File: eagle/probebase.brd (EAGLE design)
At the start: 20 x 20 mm, 11 parts, among them M1 TPTP14R, M2 TPTP14R, M3 TPTP14R, P1- TPTP14R, P2- TPTP14R, P3- TPTP14R, P4- TPTP14R

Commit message: full probe demo except for lights and antenna
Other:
- outline, holes or cut-outs redrawn
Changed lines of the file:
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@@
 <plain>
 <circle x="10" y="10" radius="10" width="0.1524" layer="20"/>
-<wire x1="3" y1="9" x2="3" y2="12" width="0.1524" layer="20"/>
-<wire x1="3" y1="12" x2="17" y2="12" width="0.1524" layer="20"/>
-<wire x1="17" y1="12" x2="17" y2="9" width="0.1524" layer="20"/>
-<wire x1="17" y1="9" x2="3" y2="9" width="0.1524" layer="20"/>
 </plain>
 <attributes>

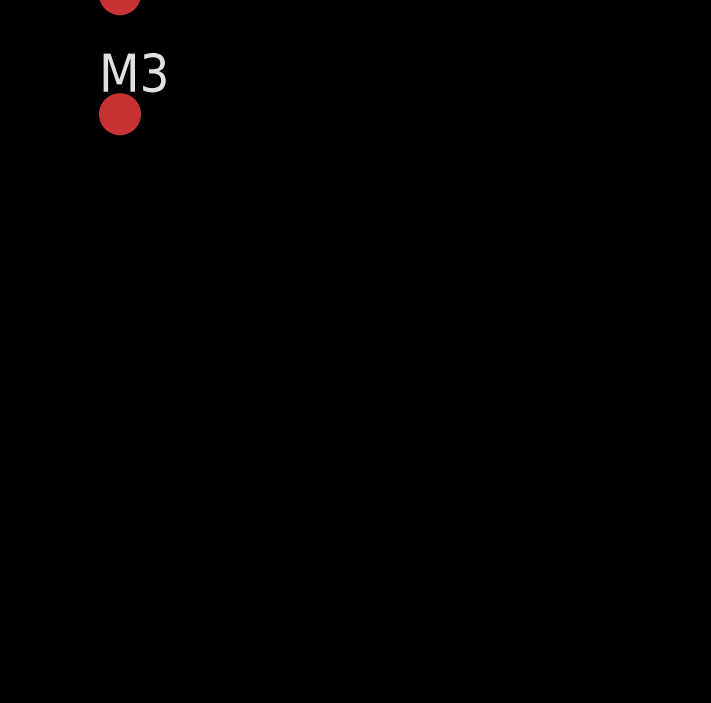
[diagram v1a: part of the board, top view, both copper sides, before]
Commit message: decided on ffc wire layout.
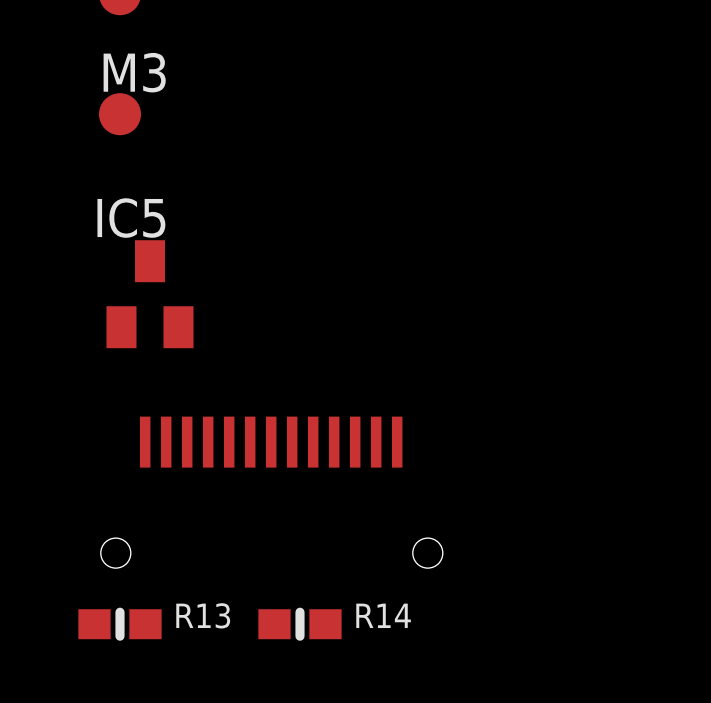
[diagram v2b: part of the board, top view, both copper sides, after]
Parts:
- added IC5: APX803, adafruit:SOT23
- added R13: 10K, microbuilder:0603-NO
- added R14: 22, microbuilder:0603-NO
- added U$4: TFT, general:MICROBUILDER_TFT_1.14IN_240X135_WRAPUNDER
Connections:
- new net !TFTRST: IC5.2, R13.1
- new net DC: U$4.5
- new net MOSI: U$4.3
- new net N$1: R14.2, U$4.11
- new net SCK: U$4.4
- new net TFTCS: U$4.7
- new net TFTRST: U$4.6
- net 3V: now also IC5.3, R13.2, U$4.10, U$4.12
- net GND: now also IC5.1, R14.1, U$4.13, U$4.8
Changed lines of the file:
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@@
 </variantdefs>
 <classes>
-<class number="0" name="default" width="0" drill="0">
+<class number="0" name="default" width="0.1524" drill="0">
+<clearance class="0" value="0.1524"/>
+</class>
+<class number="1" name="battery" width="0.3048" drill="0">
+<clearance class="1" value="0.1524"/>
 </class>
 </classes>
@@
 <attribute name="VALUE" x="0.492" y="-36.762" size="0.0254" layer="27"/>
 </element>
+<element name="IC5" library="adafruit" package="SOT23" value="APX803" x="2" y="-42" smashed="yes">
+<attribute name="NAME" x="0.095" y="-40.095" size="1.27" layer="25"/>
+<attribute name="VALUE" x="0.095" y="-45.175" size="1.27" layer="27"/>
+</element>
+<element name="R13" library="microbuilder" package="0603-NO" value="10K" x="1" y="-53" smashed="yes">
+<attribute name="NAME" x="2.778" y="-53.127" size="0.8128" layer="25" font="vector" ratio="18"/>
+<attribute name="VALUE" x="2.778" y="-53.762" size="0.4064" layer="27" font="vector" ratio="10"/>
+</element>
+<element name="R14" library="microbuilder" package="0603-NO" value="22" x="7" y="-53" smashed="yes">
+<attribute name="NAME" x="8.778" y="-53.127" size="0.8128" layer="25" font="vector" ratio="18"/>
+<attribute name="VALUE" x="8.778" y="-53.762" size="0.4064" layer="27" font="vector" ratio="10"/>
+</element>
+<element name="U$4" library="general" package="MICROBUILDER_TFT_1.14IN_240X135_WRAPUNDER" value="TFT" x="6" y="-49" smashed="yes"/>
 </elements>
 <signals>
@@
 <wire x1="15" y1="6.25" x2="15" y2="7" width="0.1524" layer="16"/>
 <via x="15" y="7" extent="1-16" drill="0.35"/>
+<contactref element="IC5" pad="1"/>
+<contactref element="U$4" pad="8"/>
+<contactref element="U$4" pad="13"/>
+<contactref element="R14" pad="1"/>
+<wire x1="5.34" y1="-46.93" x2="1.84" y2="-46.93" width="0" layer="19" extent="1-1"/>
+<wire x1="1.05" y1="-43.1" x2="1.84" y2="-46.93" width="0" layer="19" extent="1-1"/>
+<wire x1="6.15" y1="-53" x2="5.34" y2="-46.93" width="0" layer="19" extent="1-1"/>
+<wire x1="4.5" y1="5.75" x2="1.05" y2="-43.1" width="0" layer="19" extent="1-16"/>
+<wire x1="15" y1="7" x2="4.5" y2="5.75" width="0" layer="19" extent="16-16"/>
 </signal>
 <signal name="3V">
 <contactref element="LED1" pad="A"/>
 <contactref element="3V" pad="TP"/>
-<wire x1="1" y1="-4" x2="11.27" y2="16" width="0" layer="19" extent="1-1"/>
+<contactref element="R13" pad="2"/>
+<contactref element="IC5" pad="3"/>
+<contactref element="U$4" pad="12"/>
+<contactref element="U$4" pad="10"/>
+<wire x1="2.54" y1="-46.93" x2="1.85" y2="-53" width="0" layer="19" extent="1-1"/>
+<wire x1="3.94" y1="-46.93" x2="2.54" y2="-46.93" width="0" layer="19" extent="1-1"/>
+<wire x1="2" y1="-40.9" x2="2.54" y2="-46.93" width="0" layer="19" extent="1-1"/>
+<wire x1="1" y1="-4" x2="2" y2="-40.9" width="0" layer="19" extent="1-1"/>
+<wire x1="11.27" y1="16" x2="1" y2="-4" width="0" layer="19" extent="1-1"/>
 </signal>
 <signal name="P4-">
@@
 <contactref element="M3" pad="TP"/>
 </signal>
+<signal name="TFTCS">
+<contactref element="U$4" pad="7"/>
+</signal>
+<signal name="TFTRST">
+<contactref element="U$4" pad="6"/>
+</signal>
+<signal name="DC">
+<contactref element="U$4" pad="5"/>
+</signal>
+<signal name="SCK">
+<contactref element="U$4" pad="4"/>
+</signal>
+<signal name="MOSI">
+<contactref element="U$4" pad="3"/>
+</signal>
+<signal name="!TFTRST">
+<contactref element="IC5" pad="2"/>
+<contactref element="R13" pad="1"/>
+<wire x1="2.95" y1="-43.1" x2="0.15" y2="-53" width="0" layer="19" extent="1-1"/>
+</signal>
+<signal name="N$1">
+<contactref element="R14" pad="2"/>
+<contactref element="U$4" pad="11"/>
+<wire x1="3.24" y1="-46.93" x2="7.85" y2="-53" width="0" layer="19" extent="1-1"/>
+</signal>
 </signals>

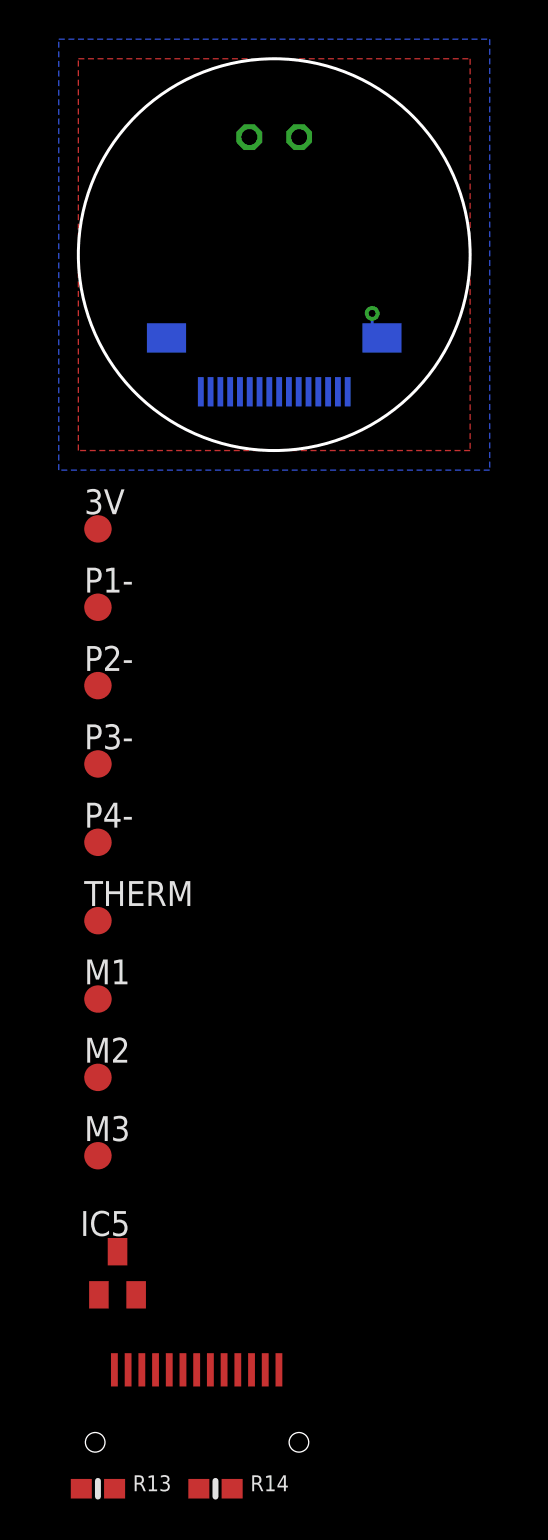
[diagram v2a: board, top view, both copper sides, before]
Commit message: First order of probe, probebase and FFC breakout PCBs for 22mm enclosure
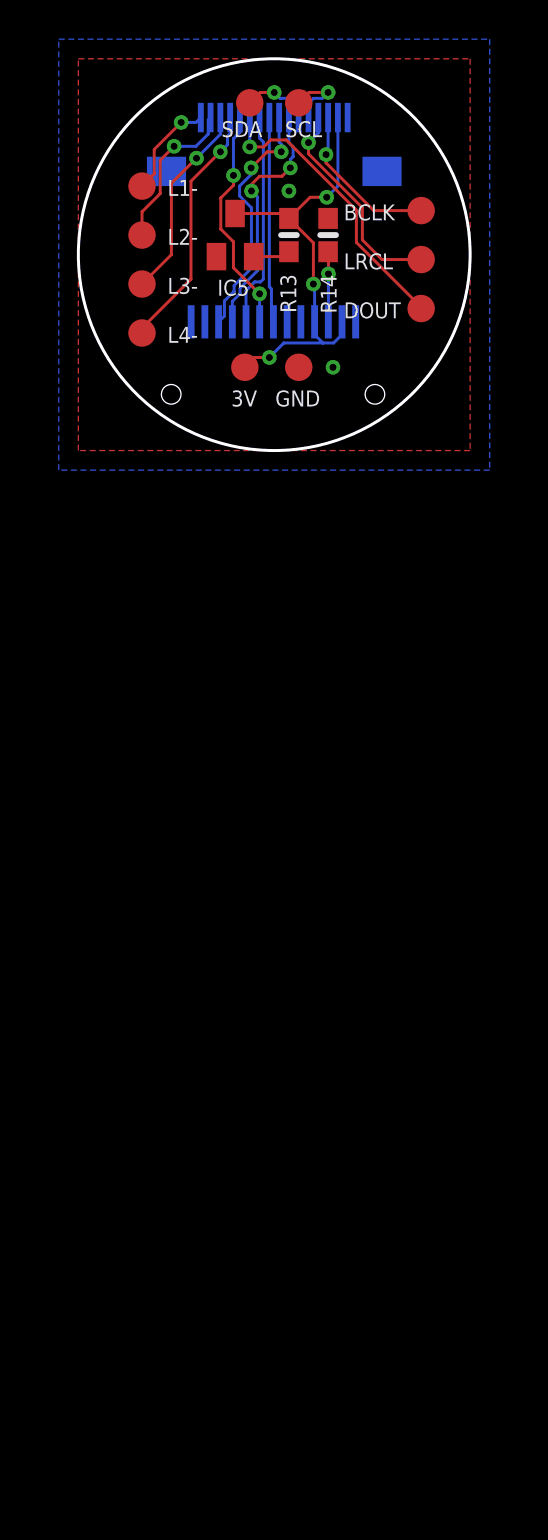
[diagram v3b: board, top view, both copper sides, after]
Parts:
- removed LED1: (no value), led:LED3MM
- removed M1, M2, M3, P1-, P2-, P3-, P4-, THERM: TPTP14R, testpad:TP14R
- removed U$1: 16PINFFC, general:16PINFFC
- added BCLK, DOUT, GND, L1-, L2-, L3-, L4-, LRCL, SCL, SDA: TPTP14R, testpad:TP14R
- added U$3: 16PINFFC, general:16PINFFC
- moved R13 64.7 mm to (10.8, 11.0), turned to 90 degrees
- moved R14 64.3 mm to (12.8, 11.0), turned to 270 degrees
- moved U$4 53.6 mm to (10.0, 4.50), flipped to the bottom
- moved IC5 53.3 mm to (8.00, 11.0)
- moved 3V 11.1 mm to (8.50, 4.25)
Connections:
- removed net M1: M1.TP
- removed net M2: M2.TP
- removed net M3: M3.TP
- removed net P1-: P1-.TP
- removed net P2-: P2-.TP
- removed net P3-: P3-.TP
- removed net P4-: LED1.K, P4-.TP
- removed net THERM: THERM.TP
- new net BCLK: BCLK.TP, U$3.14
- new net DOUT: DOUT.TP, U$3.6
- new net L1-: L1-.TP, U$3.1
- new net L2-: L2-.TP, U$3.2
- new net L3-: L3-.TP, U$3.3
- new net L4-: L4-.TP, U$3.4
- new net LRCL: LRCL.TP, U$3.13
- new net SCL: SCL.TP, U$3.12
- new net SDA: SDA.TP, U$3.11
- net 3V: now also U$3.15; no longer LED1.A
- net DC: now also U$3.7
- net GND: now also GND.TP, U$3.16, U$3.BASE1, U$3.BASE2; no longer U$1.BASE1, U$1.BASE2
- net MOSI: now also U$3.9
- net SCK: now also U$3.10
- net TFTCS: now also U$3.8
- net TFTRST: now also U$3.5
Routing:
- net 3V: track 0.00 -> 22.9 mm, vias 0 -> 3
- net DOUT: track 0.00 -> 15.0 mm, vias 0 -> 1
- net L4-: track 0.00 -> 12.9 mm, vias 0 -> 1
- net MOSI: track 0.00 -> 12.8 mm, vias 0 -> 2
- net SCK: track 0.00 -> 12.7 mm, vias 0 -> 2
- net TFTRST: track 0.00 -> 11.7 mm, vias 0 -> 2
- net DC: track 0.00 -> 11.1 mm
- net LRCL: track 0.00 -> 11.0 mm, vias 0 -> 1
- net TFTCS: track 0.00 -> 10.6 mm
- net L3-: track 0.00 -> 10.2 mm, vias 0 -> 1
- net BCLK: track 0.00 -> 8.23 mm, vias 0 -> 1
- net L2-: track 0.00 -> 8.10 mm, vias 0 -> 1
- net L1-: track 0.00 -> 5.18 mm, vias 0 -> 1
- net SDA: track 0.00 -> 3.67 mm, vias 0 -> 1
- net SCL: track 0.00 -> 3.67 mm, vias 0 -> 1
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
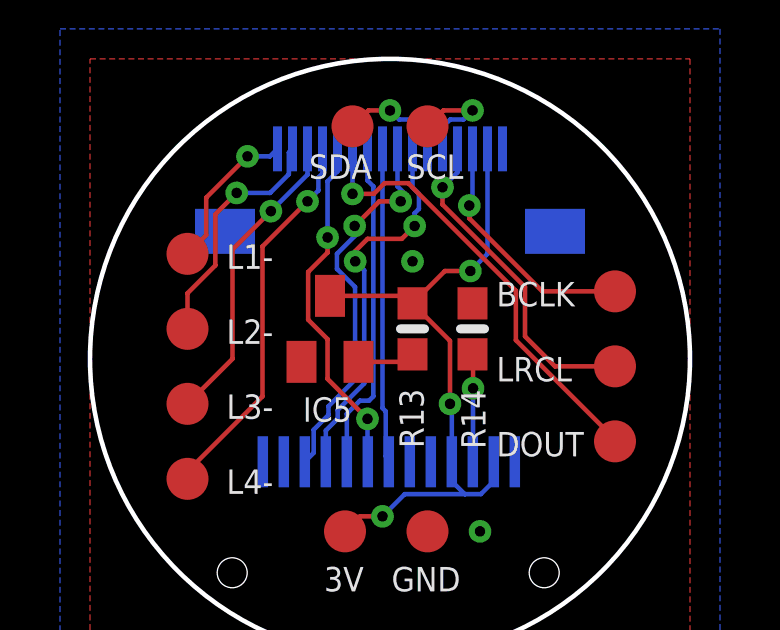
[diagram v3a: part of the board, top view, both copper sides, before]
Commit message: Fixed ffc connector dimensions
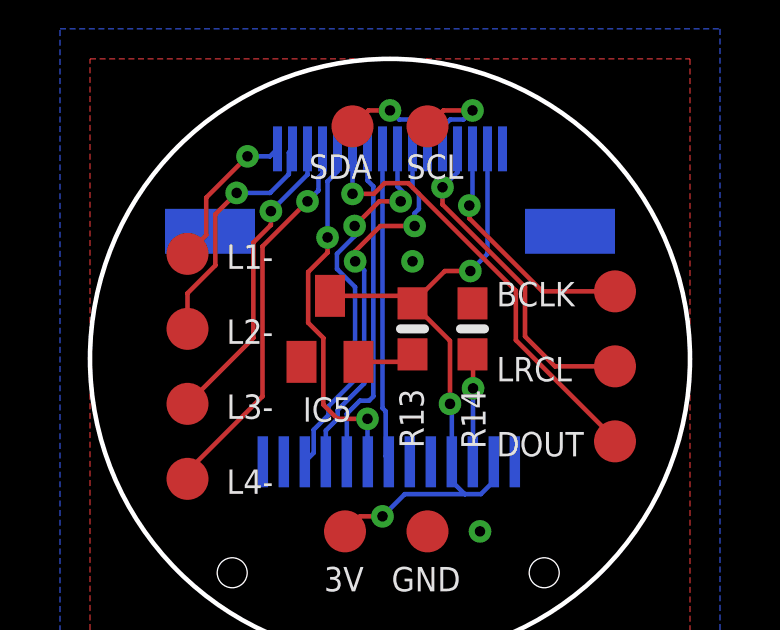
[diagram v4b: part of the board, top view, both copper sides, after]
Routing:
- net TFTRST: track 11.7 -> 12.2 mm
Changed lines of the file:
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@@
 <wire x1="9.25" y1="6.58" x2="9.25" y2="8" width="0.1524" layer="16"/>
 <via x="9.25" y="8" extent="1-16" drill="0.35"/>
-<wire x1="9.25" y1="8" x2="7.91843125" y2="9.33156875" width="0.1524" layer="1"/>
 <via x="7.91843125" y="14.04633125" extent="1-16" drill="0.35"/>
-<wire x1="7.2714" y1="11.3053125" x2="7.2714" y2="12.8946875" width="0.1524" layer="1"/>
-<wire x1="7.91843125" y1="9.33156875" x2="7.91843125" y2="10.65828125" width="0.1524" layer="1"/>
 <wire x1="7.91843125" y1="13.54171875" x2="7.91843125" y2="14.04633125" width="0.1524" layer="1"/>
-<wire x1="7.91843125" y1="10.65828125" x2="7.2714" y2="11.3053125" width="0.1524" layer="1"/>
-<wire x1="7.2714" y1="12.8946875" x2="7.91843125" y2="13.54171875" width="0.1524" layer="1"/>
+<wire x1="7.91843125" y1="13.54171875" x2="7.2714" y2="12.8946875" width="0.1524" layer="1"/>
 <wire x1="8.25" y1="17" x2="8.25" y2="16.25" width="0.1524" layer="16"/>
 <wire x1="7.91843125" y1="15.91843125" x2="7.91843125" y2="14.04633125" width="0.1524" layer="16"/>
 <wire x1="8.25" y1="16.25" x2="7.91843125" y2="15.91843125" width="0.1524" layer="16"/>
+<wire x1="7.7786" y1="8.4714" x2="8.25" y2="8" width="0.1524" layer="1"/>
+<wire x1="7.2714" y1="11.2018875" x2="7.7786" y2="10.6946875" width="0.1524" layer="1"/>
+<wire x1="7.7786" y1="10.6946875" x2="7.7786" y2="8.4714" width="0.1524" layer="1"/>
+<wire x1="8.25" y1="8" x2="9.25" y2="8" width="0.1524" layer="1"/>
+<wire x1="7.2714" y1="12.8946875" x2="7.2714" y2="11.2018875" width="0.1524" layer="1"/>
 </signal>
 <signal name="DC">
@@
 <wire x1="9.1404" y1="12.948" x2="8.8384" y2="13.25" width="0.1524" layer="16"/>
 <via x="8.8384" y="13.25" extent="1-16" drill="0.35"/>
-<wire x1="8.8384" y1="13.25" x2="8.8384" y2="13.5884" width="0.1524" layer="1"/>
-<wire x1="8.8384" y1="13.5884" x2="9.25" y2="14" width="0.1524" layer="1"/>
-<wire x1="10.3920375" y1="14" x2="10.82101875" y2="14.42898125" width="0.1524" layer="1"/>
+<wire x1="8.8384" y1="13.5884" x2="8.8384" y2="13.25" width="0.1524" layer="1"/>
 <via x="10.82101875" y="14.42898125" extent="1-16" drill="0.35"/>
 <wire x1="10.9636" y1="14.99865" x2="10.9636" y2="15.50135" width="0.1524" layer="16"/>
@@
 <wire x1="10.82101875" y1="14.42898125" x2="10.82101875" y2="14.85606875" width="0.1524" layer="16"/>
 <wire x1="10.82101875" y1="14.85606875" x2="10.9636" y2="14.99865" width="0.1524" layer="16"/>
-<wire x1="9.25" y1="14" x2="10.3920375" y2="14" width="0.1524" layer="1"/>
+<wire x1="10.82101875" y1="14.42898125" x2="9.67898125" y2="14.42898125" width="0.1524" layer="1"/>
+<wire x1="9.67898125" y1="14.42898125" x2="8.8384" y2="13.5884" width="0.1524" layer="1"/>
 </signal>
 <signal name="MOSI">
@@
 <wire x1="7.25" y1="16.1432" x2="6.0306" y2="14.9238" width="0.1524" layer="16"/>
 <via x="6.0306" y="14.9238" extent="1-16" drill="0.35"/>
-<wire x1="6.0306" y1="14.9238" x2="4.75" y2="13.6432" width="0.1524" layer="1"/>
-<wire x1="4.75" y1="10" x2="3.25" y2="8.5" width="0.1524" layer="1"/>
-<wire x1="4.75" y1="13.6432" x2="4.75" y2="10" width="0.1524" layer="1"/>
+<wire x1="6.0306" y1="14.9238" x2="6.0306" y2="14.46165625" width="0.1524" layer="1"/>
+<wire x1="6.0306" y1="14.46165625" x2="5.4452" y2="13.87625625" width="0.1524" layer="1"/>
+<wire x1="5.4452" y1="13.87625625" x2="5.4452" y2="10.6952" width="0.1524" layer="1"/>
+<wire x1="5.4452" y1="10.6952" x2="3.25" y2="8.5" width="0.1524" layer="1"/>
 </signal>
 <signal name="L4-">

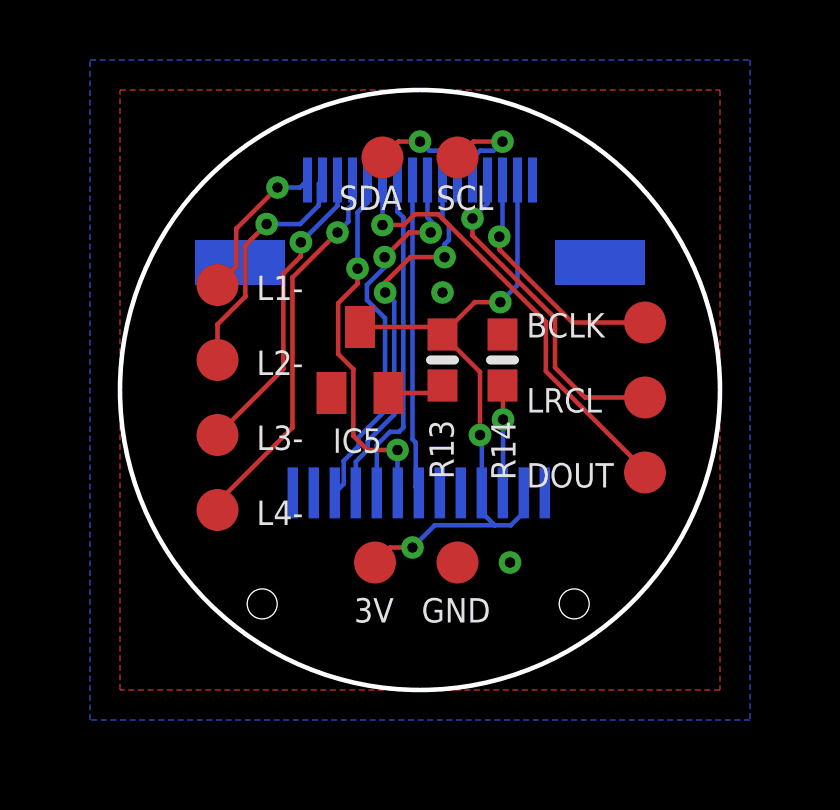
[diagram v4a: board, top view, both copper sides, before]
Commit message: Redesigned probe base pcb
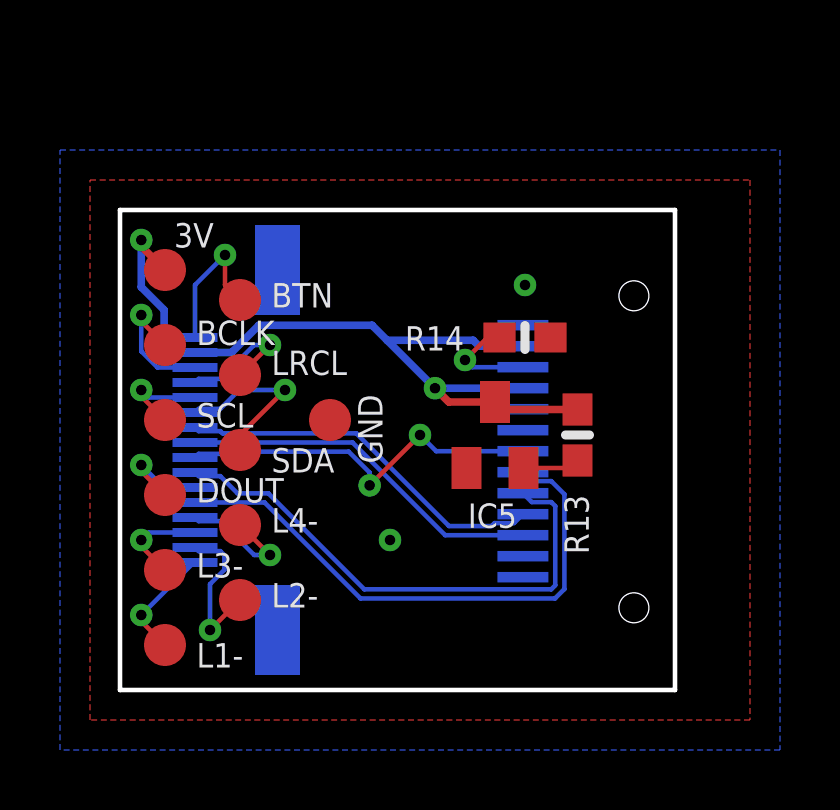
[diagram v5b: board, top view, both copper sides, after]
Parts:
- added BTN: TPTP14R, testpad:TP14R
- moved BCLK 16.0 mm to (1.50, 11.5)
- moved DOUT 16.0 mm to (1.50, 6.50)
- moved LRCL 13.5 mm to (4.00, 10.5)
- moved SCL 13.1 mm to (1.50, 9.00)
- moved L1- 12.1 mm to (1.50, 1.50)
- moved 3V 12.0 mm to (1.50, 14.0)
- moved U$3 11.7 mm to (2.50, 8.00), turned to 90 degrees
- moved SDA 10.8 mm to (4.00, 8.00)
- moved L2- 8.04 mm to (4.00, 3.00)
- moved U$4 6.52 mm to (15.5, 8.00), turned to 270 degrees
- moved GND 6.37 mm to (7.00, 9.00)
- moved IC5 5.15 mm to (12.5, 8.50)
- moved R13 5.15 mm to (15.2, 8.50)
- moved L3- 4.83 mm to (1.50, 4.00)
- moved R14 1.06 mm to (13.5, 11.8), turned to 180 degrees
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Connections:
- new net BTN: BTN.TP, U$3.16
- net GND: no longer U$3.16
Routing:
- net DOUT: track 15.0 -> 3.43 mm
- net L4-: track 12.9 -> 4.43 mm
- net L3-: track 10.2 -> 3.22 mm
- net LRCL: track 11.0 -> 4.43 mm
- net DC: track 11.1 -> 17.6 mm
- net TFTRST: track 12.2 -> 18.6 mm, vias 2 -> 0
- net 3V: track 22.9 -> 28.1 mm, vias 3 -> 2
- net BTN: track 0.00 -> 4.87 mm, vias 0 -> 1
- net BCLK: track 8.23 -> 4.55 mm
- net L2-: track 8.10 -> 5.19 mm
- net SDA: track 3.67 -> 5.93 mm
- net TFTCS: track 10.6 -> 12.6 mm, vias 0 -> 2
- net L1-: track 5.18 -> 3.84 mm
- net MOSI: track 12.8 -> 12.2 mm, vias 2 -> 0
- net SCK: track 12.7 -> 12.5 mm, vias 2 -> 0
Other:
- board size 20 x 20 mm -> 18.5 x 16 mm
